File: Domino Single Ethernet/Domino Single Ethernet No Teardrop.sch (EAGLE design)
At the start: 32 parts, among them J1 11A009-1702-00, J2 MH18-1, J3 MH18-1

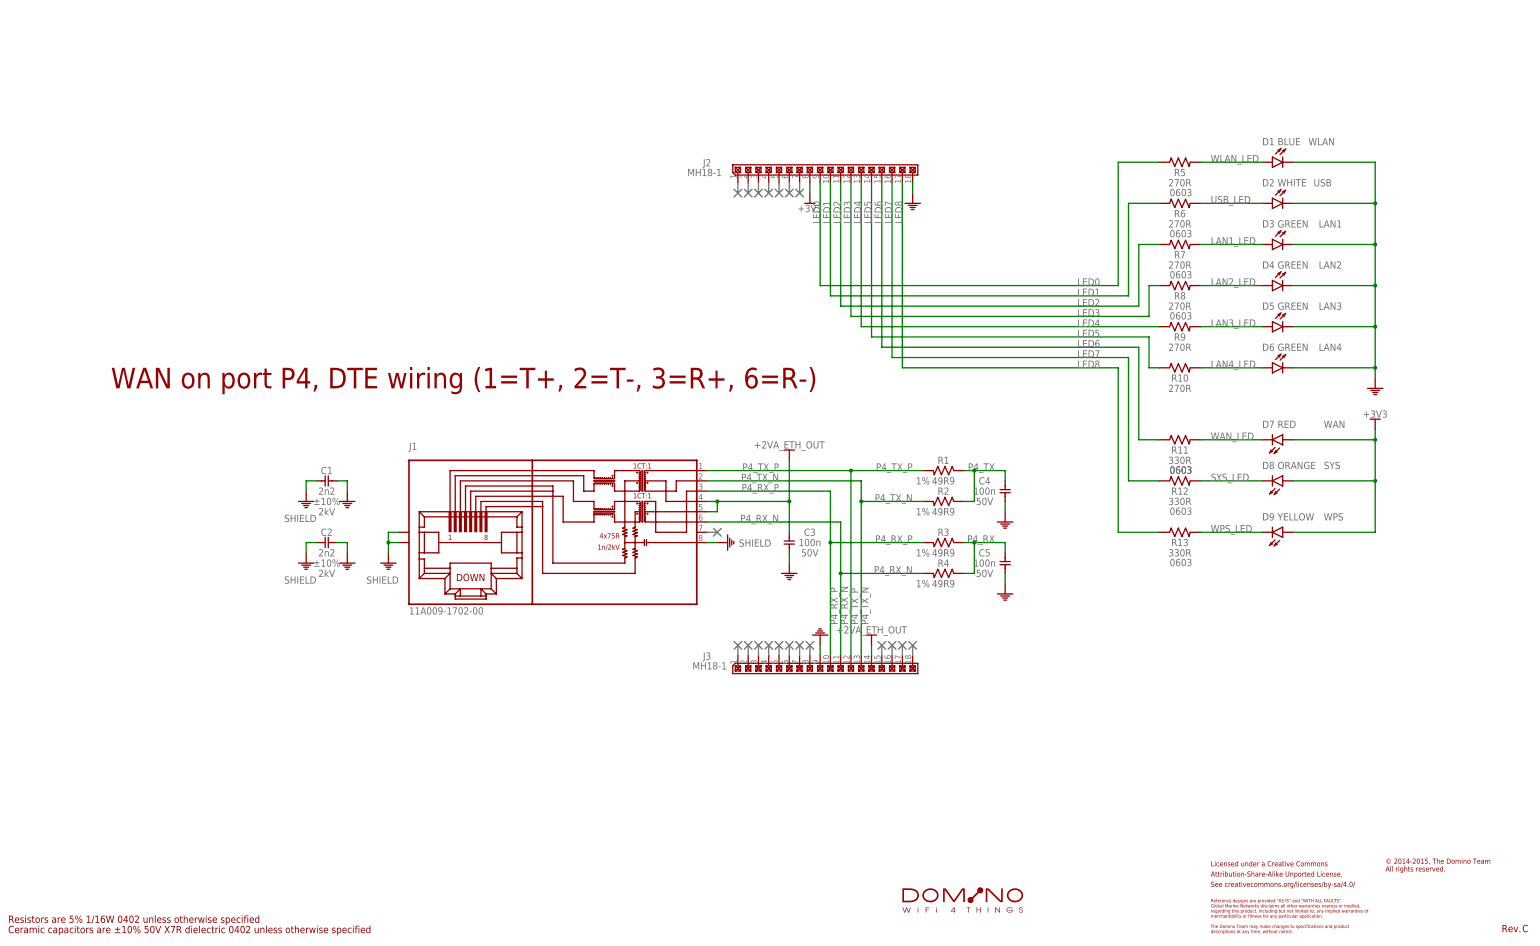
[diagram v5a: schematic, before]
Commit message: Added UART header to both Ethernet tiles
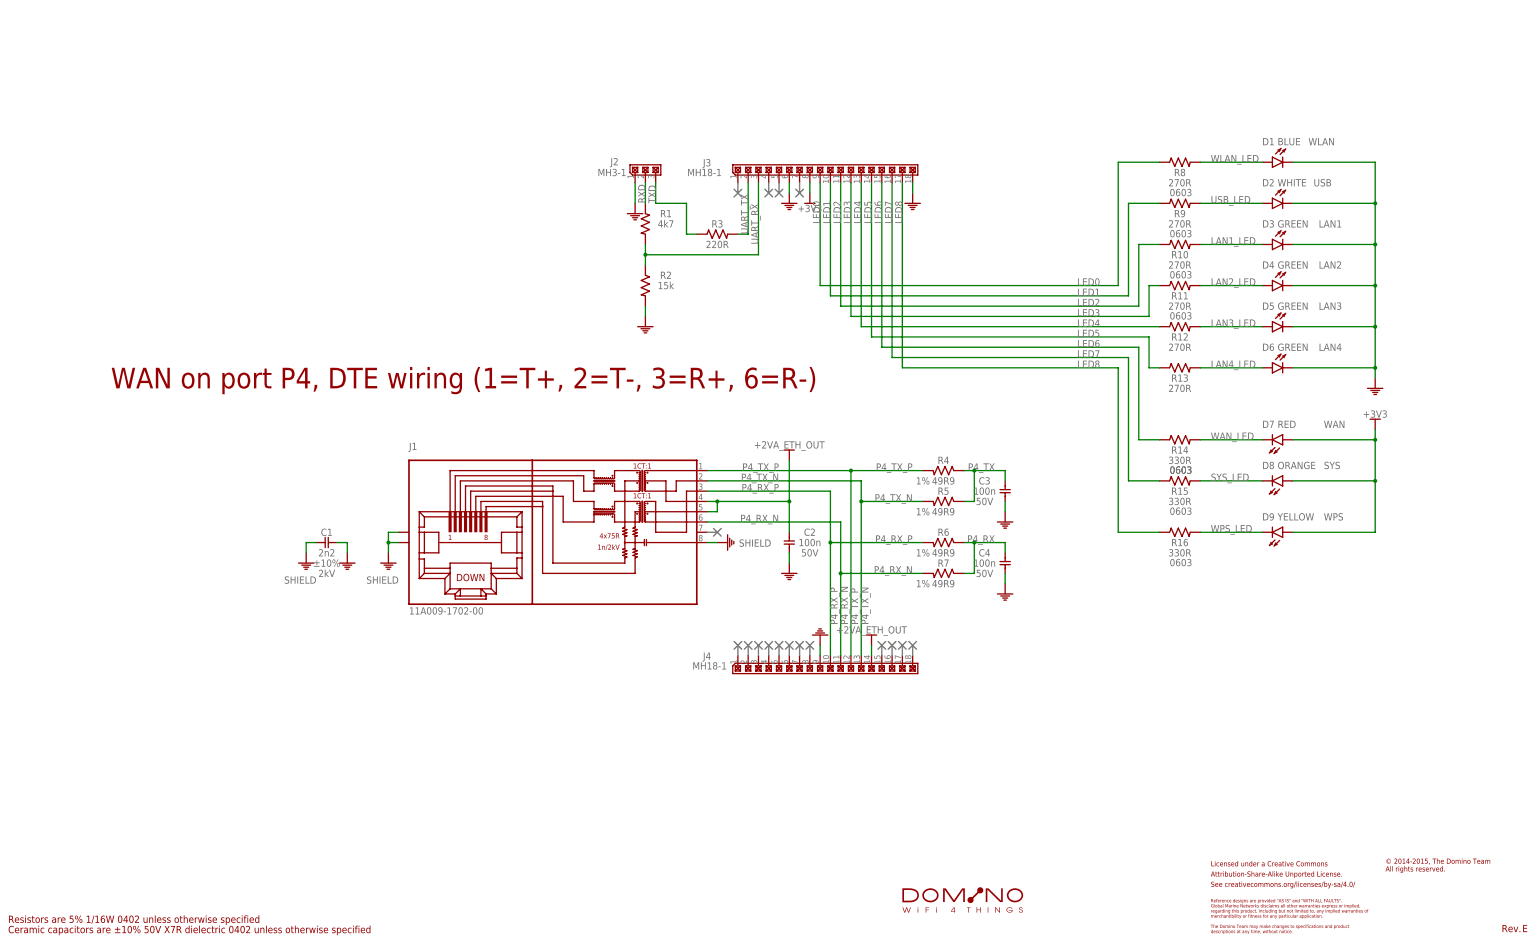
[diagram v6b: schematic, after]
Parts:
- removed C5: 100n, Domino:CAP_0402
- added J4: MH18-1, Domino:MH18-1
- added R14, R15, R16: 330R, Domino:RES_0603
- C2: value 2n2 -> 100n; device Domino:CAP_1206 -> Domino:CAP_0402; PARTNO C1210_2n2_X7R_10%_CER_2kV -> C0402_100n_X7R_10%_CER_50V; VOLT 2kV -> 50V
- J2: value MH18-1 -> MH3-1; device Domino:MH18-1 -> Domino:MH3-1; PARTNO MH18-1-0.1 -> MH3-1-0.1
- R1: value 49R9 -> 4k7; PARTNO R0402_49R9_1%_62.5mW -> R0402_4k7_5%_62.5mW; TOL 1% -> 5%
- R11, R12, R13: value 330R -> 270R; PARTNO R0603_330R_5%_125mW -> R0603_270R_5%_125mW
- R2: value 49R9 -> 15k; PARTNO R0402_49R9_1%_62.5mW -> R0402_15k_5%_62.5mW; TOL 1% -> 5%
- R3: value 49R9 -> 220R; PARTNO R0402_49R9_1%_62.5mW -> R0402_220R_5%_62.5mW; TOL 1% -> 5%
- R5, R6, R7: value 270R -> 49R9; device Domino:RES_0603 -> Domino:RES_0402; PARTNO R0603_270R_5%_125mW -> R0402_49R9_1%_62.5mW; RATE 125mW -> 62.5mW; TOL 5% -> 1%
- renumbered U$10 to L1
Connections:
- new net RXD: J2.2, R1.1
- new net TXD: J2.3, R3.1
- new net UART_RX: J3.3, R1.2, R2.1
- new net UART_TX: J3.2, R3.2
- net +2VA_ETH_OUT: now also C2.2, J4.14; no longer C3.2, J3.14
- net +3V3: now also J3.8; no longer J2.8
- net GND: now also J2.1, J3.18, J3.6, J4.9, R2.2; no longer C5.1, J2.18, J3.9
- net LAN1_LED: now also R10.2; no longer R7.2
- net LAN2_LED: now also R11.2; no longer R8.2
- net LAN3_LED: now also R12.2; no longer R9.2
- net LAN4_LED: now also R13.2; no longer R10.2
- net LED0: now also J3.9, R8.1; no longer J2.9, R5.1
- net LED1: now also J3.10, R9.1; no longer J2.10, R6.1
- net LED2: now also J3.11, R10.1; no longer J2.11, R7.1
- net LED3: now also J3.12, R11.1; no longer J2.12, R8.1
- net LED4: now also J3.13, R12.1; no longer J2.13, R9.1
- net LED5: now also J3.14, R13.1; no longer J2.14, R10.1
- net LED6: now also J3.15, R14.1; no longer J2.15, R11.1
- net LED7: now also J3.16, R15.1; no longer J2.16, R12.1
- net LED8: now also J3.17, R16.1; no longer J2.17, R13.1
- net P4_RX: now also C4.2, R6.1, R7.1; no longer C5.2, R3.1, R4.1
- net P4_RX_N: now also J4.11, R7.2; no longer J3.11, R4.2
- net P4_RX_P: now also J4.10, R6.2; no longer J3.10, R3.2
- net P4_TX: now also C3.2, R4.1, R5.1; no longer C4.2, R1.1, R2.1
- net P4_TX_N: now also J4.13, R5.2; no longer J3.13, R2.2
- net P4_TX_P: now also J4.12, R4.2; no longer J3.12, R1.2
- net SHIELD: no longer C2.2
- net SYS_LED: now also R15.2; no longer R12.2
- net USB_LED: now also R9.2; no longer R6.2
- net WAN_LED: now also R14.2; no longer R11.2
- net WLAN_LED: now also R8.2; no longer R5.2
- net WPS_LED: now also R16.2; no longer R13.2
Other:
- moved on the sheet: C1, C2, C3, C4, J3, R1, R10, R11, R12, R13, R2, R3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
